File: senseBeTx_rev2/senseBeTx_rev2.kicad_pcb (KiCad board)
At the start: 2 copper layers, 40 x 80 mm, 42 parts, among them P1 CONN_02X05, Q1 BC847, Q2 SI2301, Q3 SI2302, Q4 SI2302, Q5 SI2302, Q6 SI2302, Q7 SI2302, Q8 SI2302, Q9 SI2302, SW1 SW_Push_Dual, U1 STM32L011F3Px, Y1 Crystal

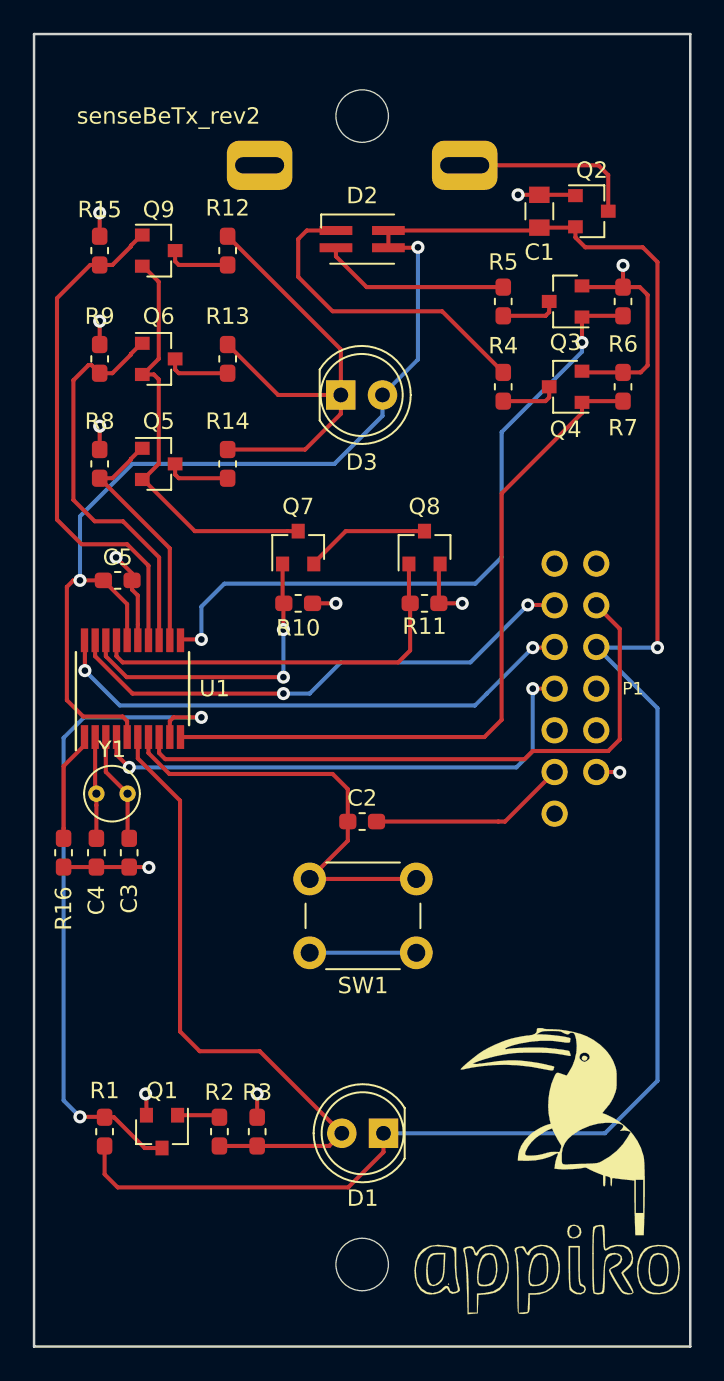
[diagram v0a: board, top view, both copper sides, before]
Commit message: Update the PCB to reduce the number of vias and add top layer copper
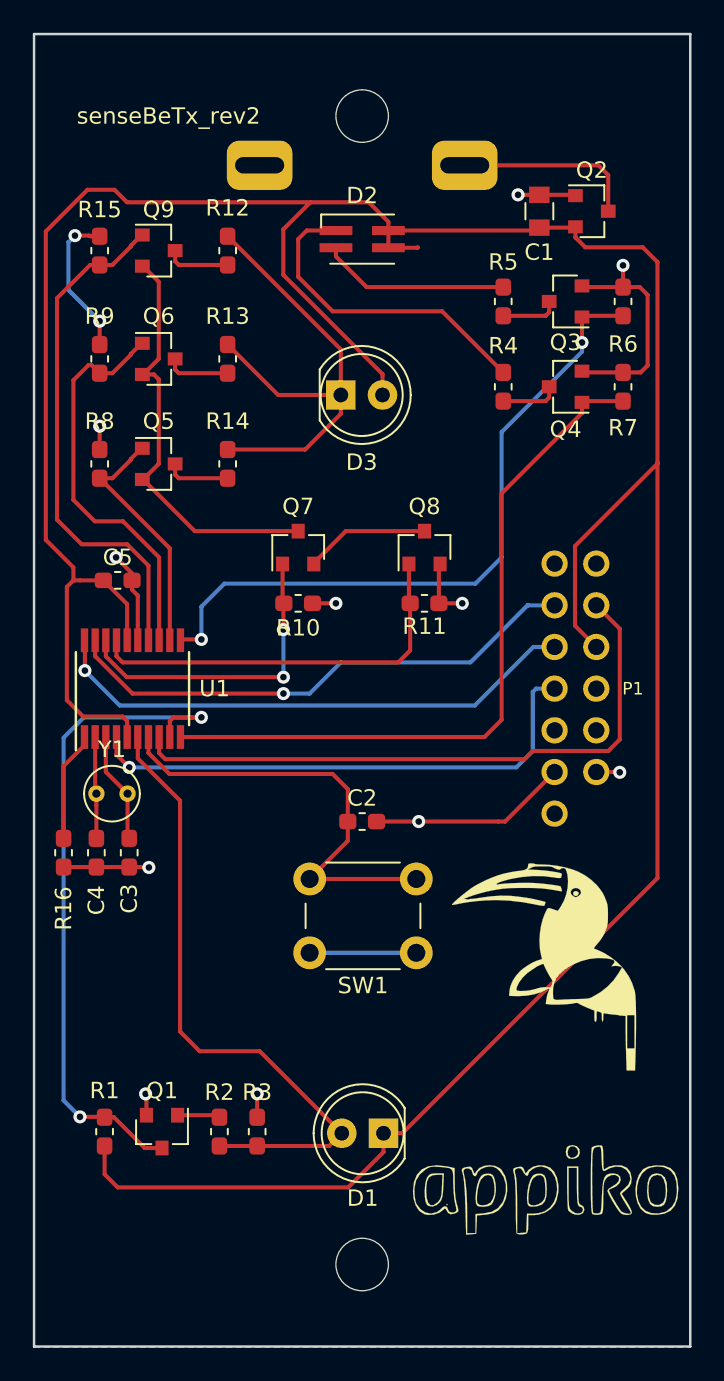
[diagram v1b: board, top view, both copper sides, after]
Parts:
- moved G*** 10.1 mm to (44.1, 173.9)
- moved G*** 4.85 mm to (41.9, 187.5)
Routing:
- net VDD: track 169.7 -> 195.2 mm, vias 3 -> 0
- net GND: track 60.7 -> 67.0 mm, vias 12 -> 13
- net /RESET: track 32.3 -> 32.2 mm, vias 2 -> 1
- net /SYS_SWDCLK: track 32.8 -> 32.9 mm, vias 2 -> 1
- net /SYS_SWDIO: vias 2 -> 1
- added copper zone on F.Cu, net GND
